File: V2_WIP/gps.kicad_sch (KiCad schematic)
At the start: 37 parts, among them J1 I2C/BATT_H, J12 ENC+RGB, J13 ENC+RGB, J2 I2C/BATT_S, J4 BATT, J5 ESP, J7 USB_B_Micro, J9 USB_pads, SW1 RotaryEncoder_Switch, SW2 MSN22AFW01, U10 24C32, U11 SN74LV1T34DBVRG4, U3 DFR0654, U9 TCA39306DDFR

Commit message: Cleaned schematic
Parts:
- removed C10, C9: 100nF, Capacitor_SMD:C_0805_2012Metric_Pad1.18x1.45mm_HandSolder, symbol Device:C
- removed J1: I2C/BATT_H, Connector_PinHeader_2.54mm:PinHeader_1x07_P2.54mm_Vertical, symbol Connector_Generic:Conn_01x07
- removed J12: ENC+RGB, Connector_PinSocket_2.54mm:PinSocket_1x06_P2.54mm_Vertical, symbol Connector_Generic:Conn_01x06
- removed J13: ENC+RGB, Connector_PinHeader_2.54mm:PinHeader_1x06_P2.54mm_Vertical, symbol Connector_Generic:Conn_01x06
- removed J2: I2C/BATT_S, Connector_PinSocket_2.54mm:PinSocket_1x07_P2.54mm_Vertical, symbol Connector_Generic:Conn_01x07
- removed J5: ESP, Connector_PinSocket_2.54mm:PinSocket_1x02_P2.54mm_Vertical, symbol Connector_Generic:Conn_01x02
- removed J7: USB_B_Micro, KiCad:USB3145301A, symbol Connector:USB_B_Micro
- removed J9: USB_pads, Connector_PinSocket_2.54mm:PinSocket_1x03_P2.54mm_Vertical, symbol Connector_Generic:Conn_01x03
- removed R3, R4, R5, R6: 4k7, Resistor_SMD:R_0805_2012Metric_Pad1.20x1.40mm_HandSolder, symbol Device:R
- removed RS1: 200k, Resistor_SMD:R_0805_2012Metric_Pad1.20x1.40mm_HandSolder, symbol Device:R
- removed TP8: DT, TestPoint:TestPoint_Pad_D1.5mm, symbol Connector:TestPoint
- removed U11: SN74LV1T34DBVRG4, Package_TO_SOT_SMD:SOT-23-5, symbol Logic_LevelTranslator:SN74LV1T34DBV
- removed U9: TCA39306DDFR, Package_TO_SOT_SMD:SOT-23-8, symbol shifter:TCA39306DCURQ1
- added C4, C5, C6: 10uF, Capacitor_SMD:C_0603_1608Metric_Pad1.08x0.95mm_HandSolder, symbol Device:C
- added D2: B120-E3, Diode_SMD:D_SMA, symbol Diode:B120-E3
- added L1: 2.2 uH, Inductor_SMD:L_1008_2520Metric_Pad1.43x2.20mm_HandSolder, symbol Device:L
- added R1: 0R, Resistor_SMD:R_0805_2012Metric_Pad1.20x1.40mm_HandSolder, symbol Device:R
- added TP3: RGB_7seg, TestPoint:TestPoint_Pad_D1.5mm, symbol Connector:TestPoint
- added TP4: DT, TestPoint:TestPoint_Pad_D1.5mm, symbol Connector:TestPoint
- added TP5: +5V, TestPoint:TestPoint_Pad_D1.5mm, symbol Connector:TestPoint
- added U2: TPS613222ADBVR, Package_TO_SOT_SMD:SOT-23-5, symbol Regulator_Switching:TPS613226ADBV
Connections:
- net +5V: now also R1.2
- net DT: now also TP4.1
- net GND: now also C4.2, C5.2, C6.2, U2.2 (GND)
- net VCC: now also C4.1, L1.1
- net GNSS_RXD renamed GNSS_RxD
- net GNSS_TXD renamed GNSS_TxD
- net PULSE renamed Pulse
- net RGB_3V3 renamed RGB
- net RGB: now also TP3.1
- net SCL_3V3 renamed SCL_ESP
- net SCL_5V renamed SCL_Display
- net SDA_3V3 renamed SDA_ESP
- net SDA_5V renamed SDA_Display
- net SW_BATT: no longer names the net of J4.1 (Pin_1), SW2.2 (B)
- net SW_ESP renamed VBATT
- new net: C5.1, C6.1, D2.1 (K), R1.1, TP5.1, U2.4 (VOUT)
- new net: D2.2 (A), L1.2, U2.1 (SW)
- no-connect marks 15 -> 14
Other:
- added sheet ESP (ESP.kicad_sch)
- added sheet I2C_Level_Shifter (Level_Shifter.kicad_sch)
- sheet Display ports: added RGB_5V, SCL_5V, SDA_5V; removed none
- sheet GNSS: file ESP.kicad_sch -> GNSS.kicad_sch
- sheet GNSS ports: added Pulse, RxD, TxD; removed none
- note added: "DC/DC"
- note removed: "Board connection 1/2"
- note removed: "Board connection 2/2"
- note removed: "RGB 7seg Level shifter"
- note removed: "USB Connector"
- note removed: "WRONG FOOTPRINT"
- moved on the sheet: C8, J4, R17, R18, R19, R_E1, R_E2, R_E3, SW1, SW2A, TP9, U10

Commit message: minor schematic changes
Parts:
- SW1: value RotaryEncoder_Switch -> RotaryEncoder
- TP10, TP11: now not fitted
- TP3: value RGB_7seg -> RGB_3V3
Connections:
- net SCL_ESP: no longer U3.29 (SCL), U3.9 (SCL)
- net SDA_ESP: no longer U3.10 (SDA), U3.28 (SDA)
- net SCL_Display renamed Display/SCL_5V
- net SDA_Display renamed Display/SDA_5V
- new net I2C_Level_Shifter/SCL_A: U3.29 (SCL), U3.9 (SCL)
- new net I2C_Level_Shifter/SDA_A: U3.10 (SDA), U3.28 (SDA)
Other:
- sheet Display ports: added RGB_3V3; removed RGB_5V
- moved on the sheet: C4, C5, C6, C8, J4, L1, R1, R17, R18, R19, R_E3, SW2A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

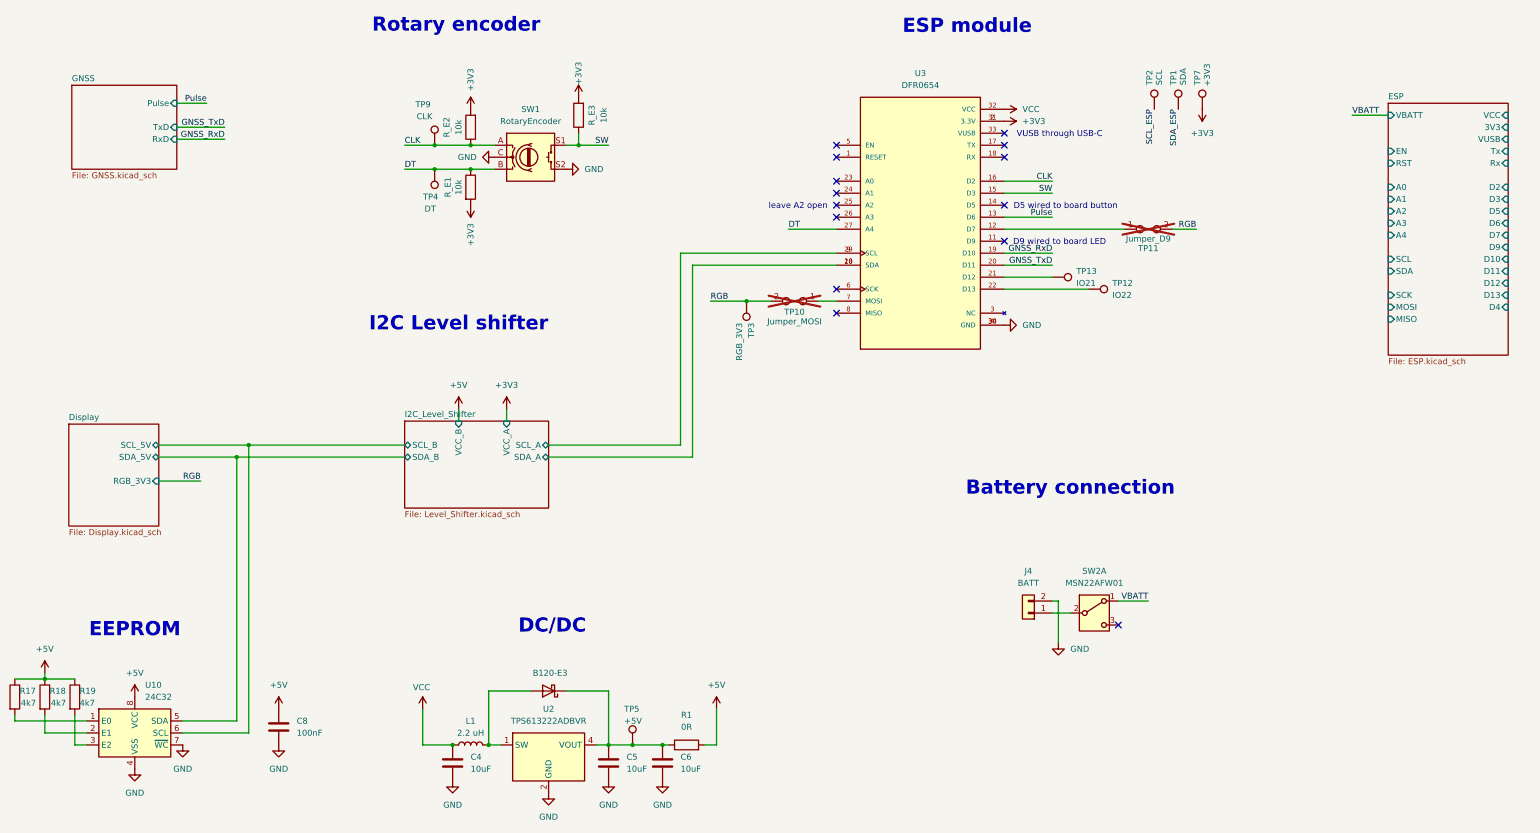
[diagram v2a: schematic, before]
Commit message: switched esp modul symbol for esp sheet
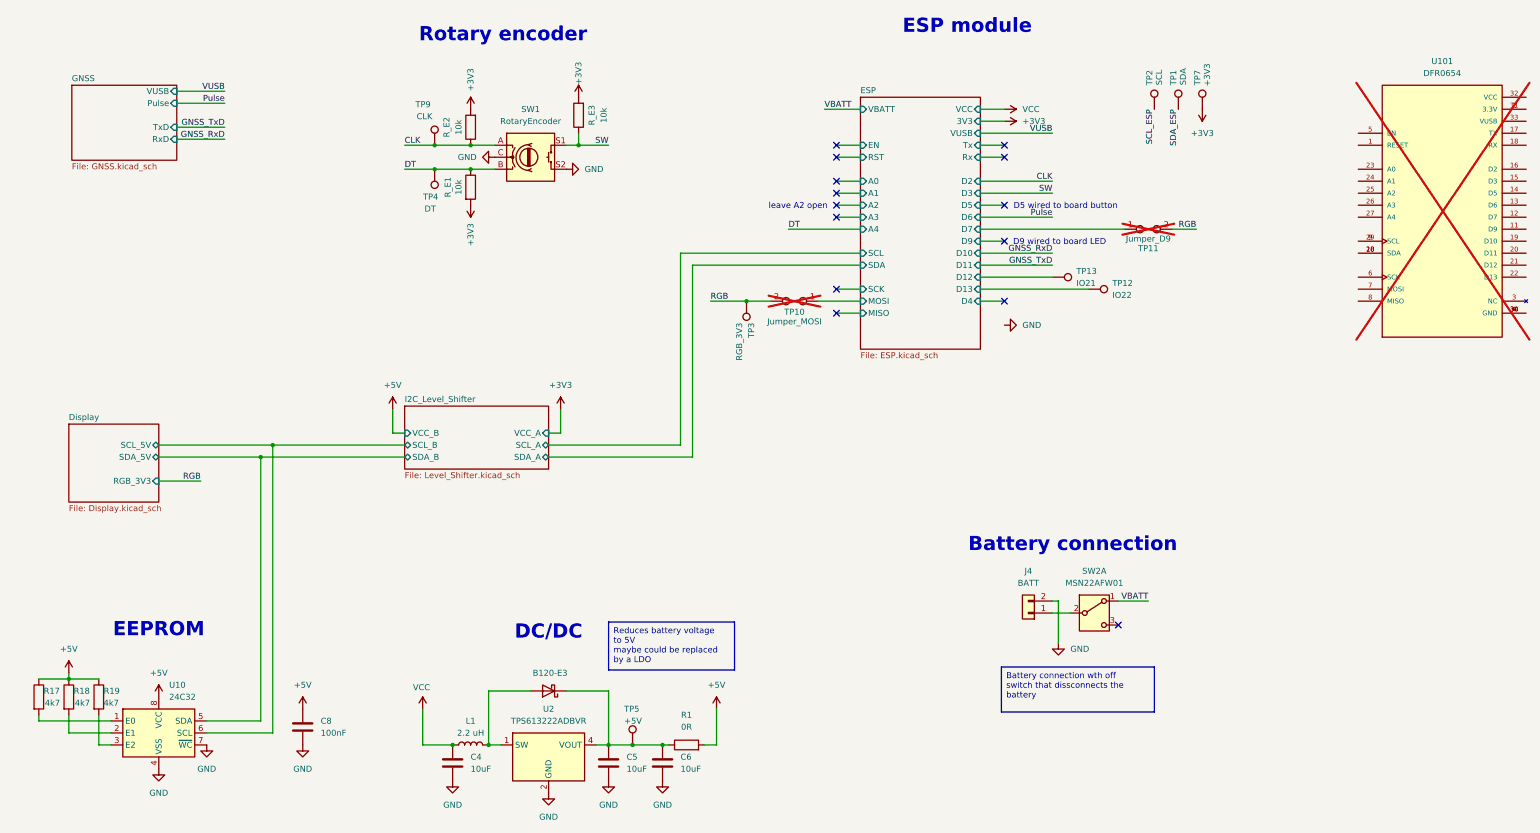
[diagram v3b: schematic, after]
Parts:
- removed U3: DFR0654, DFR0654:DFR0654_2, symbol DFR0654:DFR0654
- added U101: DFR0654, DFR0654:DFR0654_2, symbol DFR0654:DFR0654
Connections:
- net ESP/D12: now also TP13.1
- net ESP/D13: now also TP12.1
- net ESP/D7: now also TP11.1
- net ESP/MOSI: now also TP10.1
- new net: U101.10 (SDA), U101.28 (SDA)
- new net: U101.2 (3.3V), U101.31 (3.3V)
- new net: U101.29 (SCL), U101.9 (SCL)
- new net: U101.30 (GND), U101.34 (GND), U101.4 (GND)
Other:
- sheet GNSS ports: added VUSB; removed none
- note removed: "I2C Level shifter"
- note removed: "VUSB through USB-C"
- moved on the sheet: C8, R17, R18, R19, U10

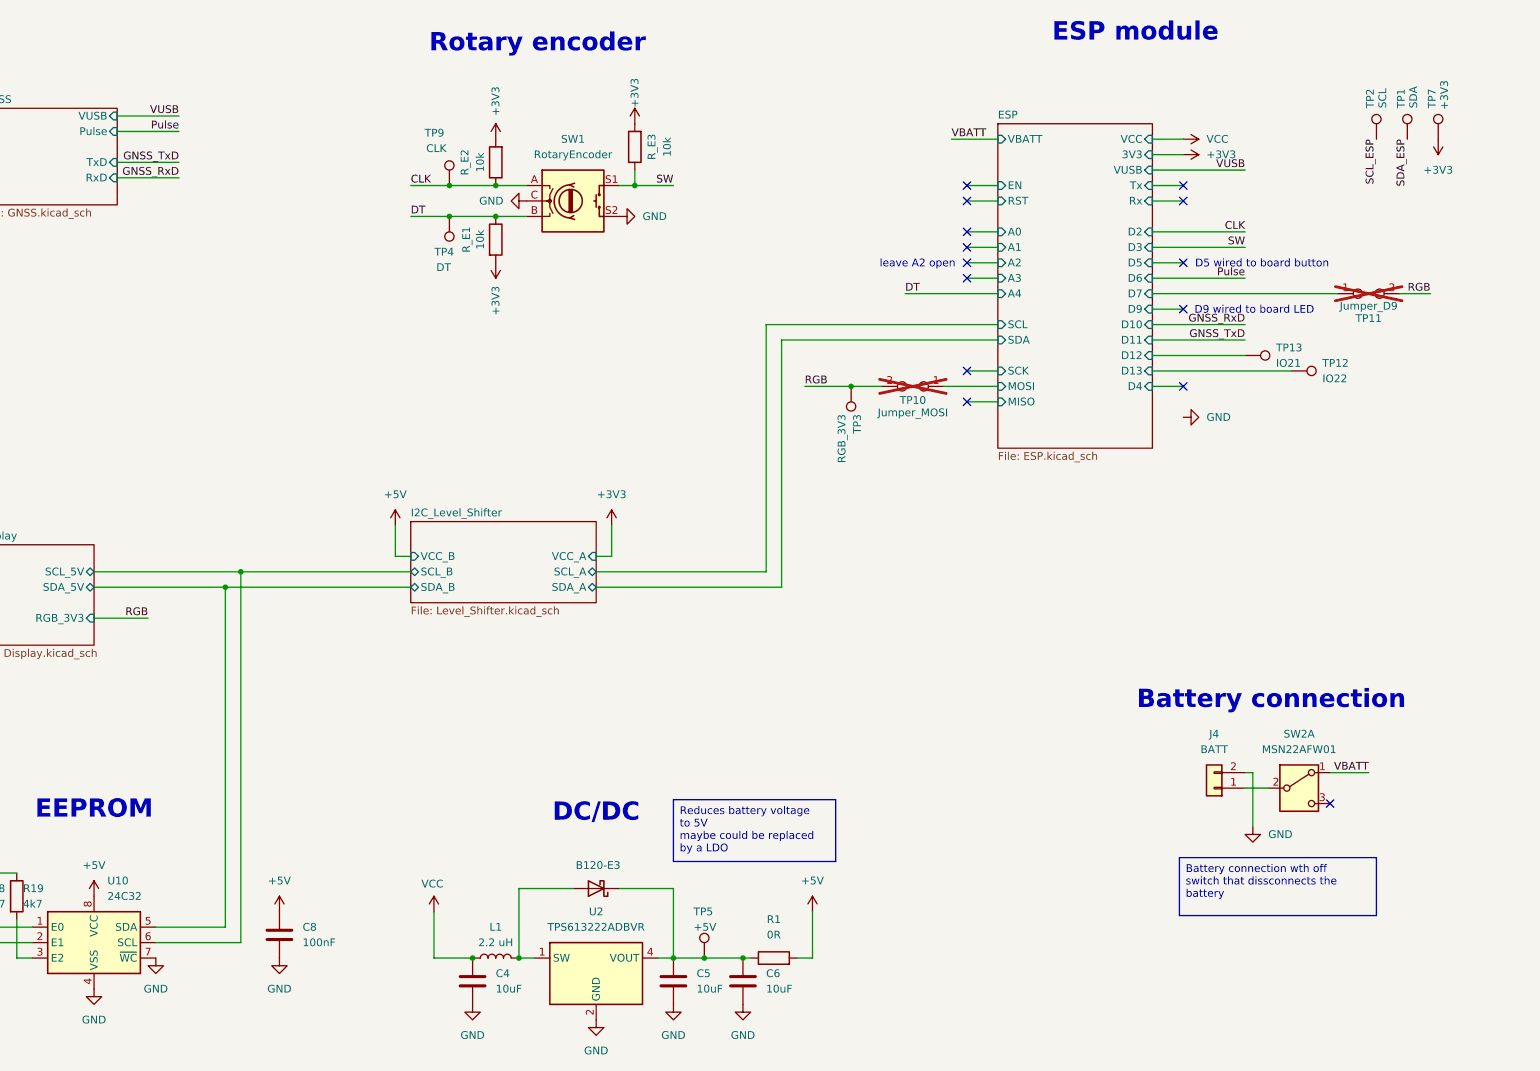
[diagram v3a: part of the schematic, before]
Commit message: added LED indicators, light sensor, changed to CC 7seg displays
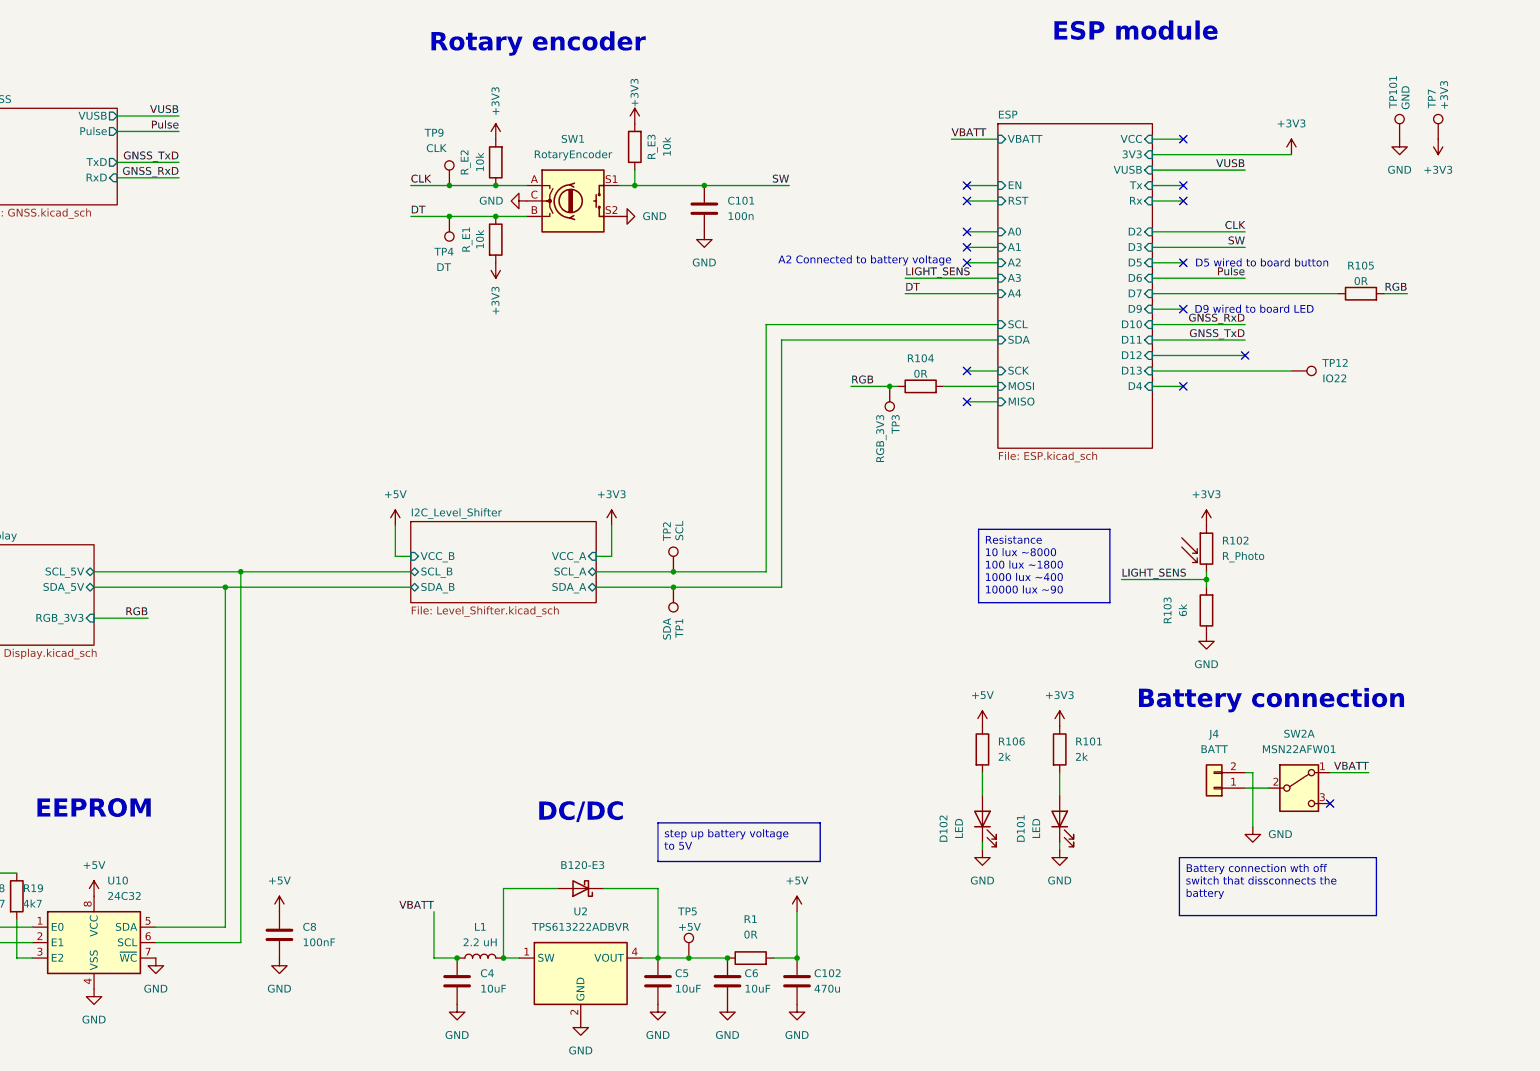
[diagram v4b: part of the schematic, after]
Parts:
- removed TP10: Jumper_MOSI, Resistor_SMD:R_0805_2012Metric_Pad1.20x1.40mm_HandSolder, symbol Connector:TestPoint_2Pole
- removed TP11: Jumper_D9, Resistor_SMD:R_0805_2012Metric_Pad1.20x1.40mm_HandSolder, symbol Connector:TestPoint_2Pole
- removed TP13: IO21, TestPoint:TestPoint_Pad_D1.5mm, symbol Connector:TestPoint
- added C101: 100n, Capacitor_SMD:C_0603_1608Metric_Pad1.08x0.95mm_HandSolder, symbol Device:C
- added C102: 470u, Capacitor_SMD:C_0603_1608Metric_Pad1.08x0.95mm_HandSolder, symbol Device:C
- added D101, D102: LED, LED_THT:LED_D3.0mm, symbol Device:LED
- added R101, R106: 2k, Resistor_SMD:R_0603_1608Metric_Pad0.98x0.95mm_HandSolder, symbol Device:R
- added R102: R_Photo, OptoDevice:R_LDR_5.1x4.3mm_P3.4mm_Vertical, symbol Device:R_Photo
- added R103: 6k, Resistor_SMD:R_0603_1608Metric_Pad0.98x0.95mm_HandSolder, symbol Device:R
- added R104, R105: 0R, Resistor_SMD:R_0805_2012Metric_Pad1.20x1.40mm_HandSolder, symbol Device:R
- added TP101: GND, TestPoint:TestPoint_THTPad_D2.5mm_Drill1.2mm, symbol Connector:TestPoint
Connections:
- net SCL_ESP is gone; now on net ESP/SCL: TP2.1
- net SDA_ESP is gone; now on net ESP/SDA: TP1.1
- net VCC is gone; now on net VBATT: C4.1, L1.1
- net +3V3: now also R101.1, R102.1
- net +5V: now also C102.1, R106.1
- net ESP/D7: now also R105.1
- net ESP/MOSI: now also R104.2
- net GND: now also C101.2, C102.2, D101.1 (K), D102.1 (K), R103.1, TP101.1
- net RGB: now also R104.1, R105.2
- net SW: now also C101.1
- new net: D102.2 (A), R106.2
- new net: D101.2 (A), R101.2
- new net LIGHT_SENS: R102.2, R103.2
- no-connect marks 14 -> 15
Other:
- note added: "A2 Connected to battery voltage"
- note removed: "leave A2 open"
- moved on the sheet: C4, C5, C6, L1, R1, TP1, TP2, TP3, TP5, U2
